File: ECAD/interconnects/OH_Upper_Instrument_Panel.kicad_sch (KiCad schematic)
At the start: 194 parts

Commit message: Closed issue #987, #988, & #992
Updated interconnect and PL.
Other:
- note added: "3.0 IN PIGTAILS ON 1A7A1J1/J2"

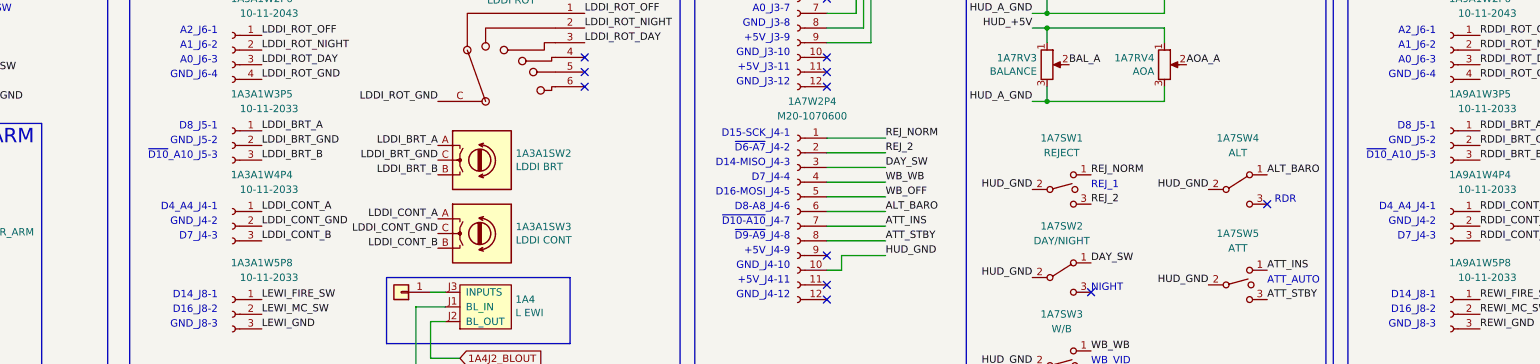
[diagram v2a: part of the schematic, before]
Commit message: Updated interconnect.
Made FCS_+5V NC
Reversed DDI BRT/CONT connections so they align properly with the PCB.
Closes #990 & #993
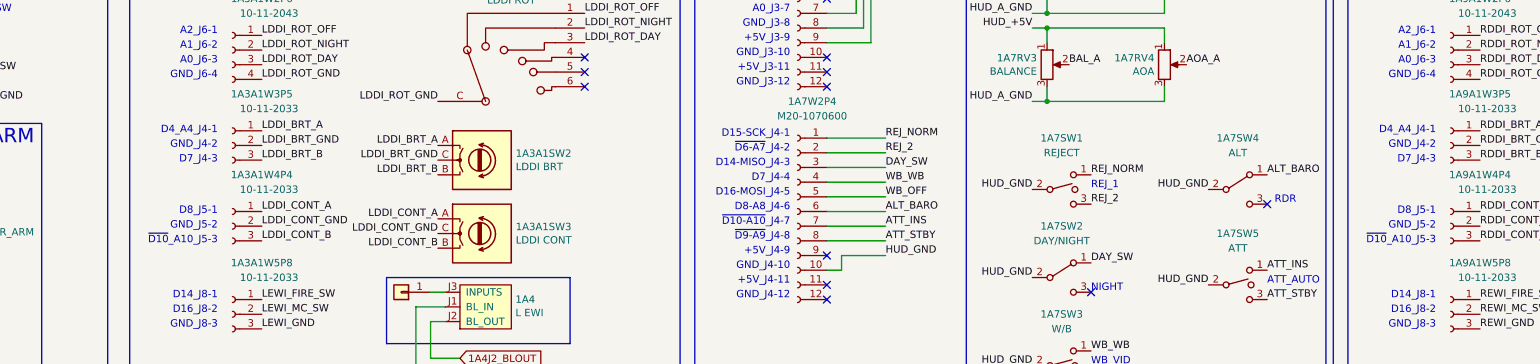
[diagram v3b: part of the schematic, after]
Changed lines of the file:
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@@
     (effects (font (size 1.27 1.27)) (justify right bottom))
   )
-  (text "~{D10}_A10_J5-3" (at 308.61 288.29 0)
+  (text "~{D10}_A10_J5-3" (at 308.61 302.895 0)
     (effects (font (size 1.27 1.27)) (justify right bottom))
   )
@@
     (effects (font (size 1.27 1.27)) (justify left bottom))
   )
-  (text "D8_J5-1" (at 519.43 283.21 0)
+  (text "D8_J5-1" (at 519.43 297.815 0)
     (effects (font (size 1.27 1.27)) (justify right bottom))
   )
@@
     (effects (font (size 1.27 1.27)) (justify right bottom))
   )
-  (text "D8_J5-1" (at 308.61 283.21 0)
+  (text "D8_J5-1" (at 308.61 297.815 0)
     (effects (font (size 1.27 1.27)) (justify right bottom))
   )
@@
     (effects (font (size 1.27 1.27)) (justify left bottom))
   )
-  (text "GND_J4-2" (at 519.43 299.72 0)
+  (text "GND_J4-2" (at 519.43 286.385 0)
     (effects (font (size 1.27 1.27)) (justify right bottom))
   )
@@
     (effects (font (size 1.27 1.27)) (justify right bottom))
   )
-  (text "D4_A4_J4-1" (at 308.61 297.18 0)
+  (text "D4_A4_J4-1" (at 308.61 283.845 0)
     (effects (font (size 1.27 1.27)) (justify right bottom))
   )
@@
     (effects (font (size 1.27 1.27)) (justify right bottom))
   )
-  (text "GND_J4-2" (at 308.61 299.72 0)
-    (effects (font (size 1.27 1.27)) (justify right bottom))
-  )
-  (text "D4_A4_J4-1" (at 519.43 297.18 0)
+  (text "GND_J4-2" (at 308.61 286.385 0)
+    (effects (font (size 1.27 1.27)) (justify right bottom))
+  )
+  (text "D4_A4_J4-1" (at 519.43 283.845 0)
     (effects (font (size 1.27 1.27)) (justify right bottom))
   )
@@
     (effects (font (size 1.27 1.27)) (justify left bottom))
   )
-  (text "~{D10}_A10_J5-3" (at 519.43 288.29 0)
+  (text "~{D10}_A10_J5-3" (at 519.43 302.895 0)
     (effects (font (size 1.27 1.27)) (justify right bottom))
   )
@@
     (effects (font (size 2.4892 2.4892)) (justify left bottom))
   )
-  (text "GND_J5-2" (at 308.61 285.75 0)
+  (text "GND_J5-2" (at 308.61 300.355 0)
     (effects (font (size 1.27 1.27)) (justify right bottom))
   )
@@
     (effects (font (size 1.27 1.27)) (justify left bottom))
   )
-  (text "D7_J4-3" (at 308.61 302.26 0)
+  (text "D7_J4-3" (at 308.61 288.925 0)
     (effects (font (size 1.27 1.27)) (justify right bottom))
   )
@@
     (effects (font (size 1.27 1.27)) (justify right bottom))
   )
-  (text "D7_J4-3" (at 519.43 302.26 0)
+  (text "D7_J4-3" (at 519.43 288.925 0)
     (effects (font (size 1.27 1.27)) (justify right bottom))
   )
@@
     (effects (font (size 1.27 1.27)) (justify right bottom))
   )
-  (text "GND_J5-2" (at 519.43 285.75 0)
-    (effects (font (size 1.27 1.27)) (justify right bottom))
-  )
+  (text "GND_J5-2" (at 519.43 300.355 0)
+    (effects (font (size 1.27 1.27)) (justify right bottom))
+  )

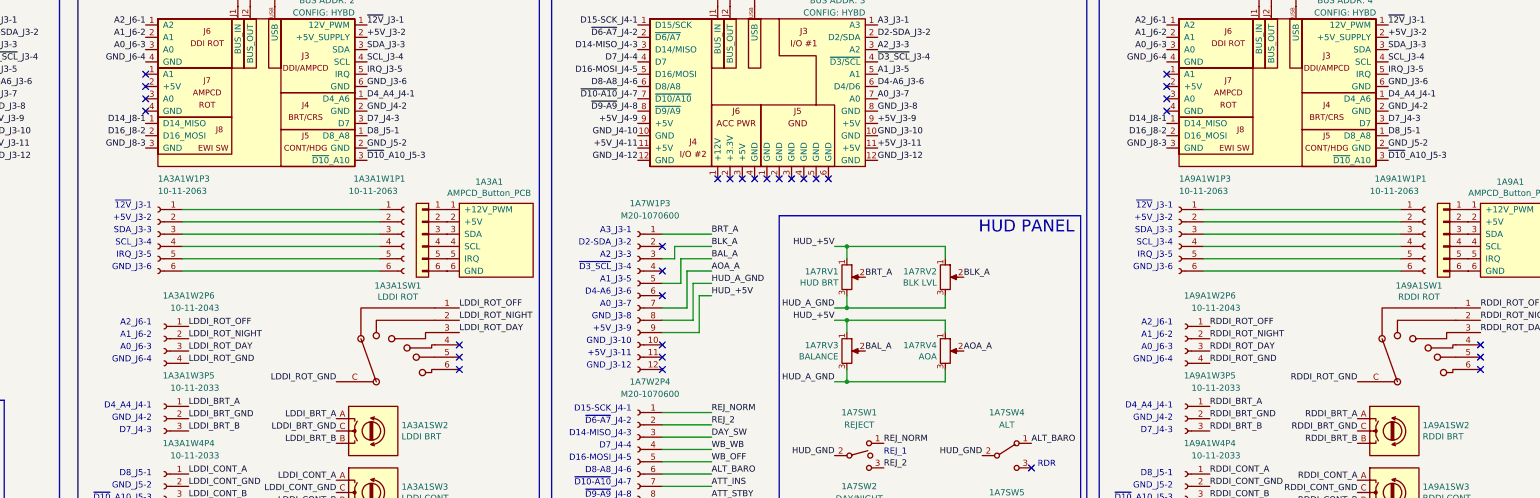
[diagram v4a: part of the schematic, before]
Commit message: Updated L/R-DDI and AMPCD controller net labels.
Revised interconnect to Rev A

1. SH 2:
    1. 1A3J4 Pin 1 WAS: D4_A4_J4-1 / IS: D4_A6_J4-1
    2. 1A3A1W3P5 Pin 1 WAS: D4_A4_J4-1 / IS: D4_A6_J4-1
    3. 1A9J4 Pin 1 WAS: D4_A4_J4-1 / IS: D4_A6_J4-1
    4. 1A9A1W3P5 Pin 1 WAS: D4_A4_J4-1 / IS: D4_A6_J4-1

2. SH 3:
    1. 2A3A1J4 Pin 1 WAS: D4_A4_J4-1 / IS: D4_A6_J4-1
    2. 2A3A1W4P1 Pin 1 WAS: D4_A4_J4-1 / IS: D4_A6_J4-1

Closes #1031
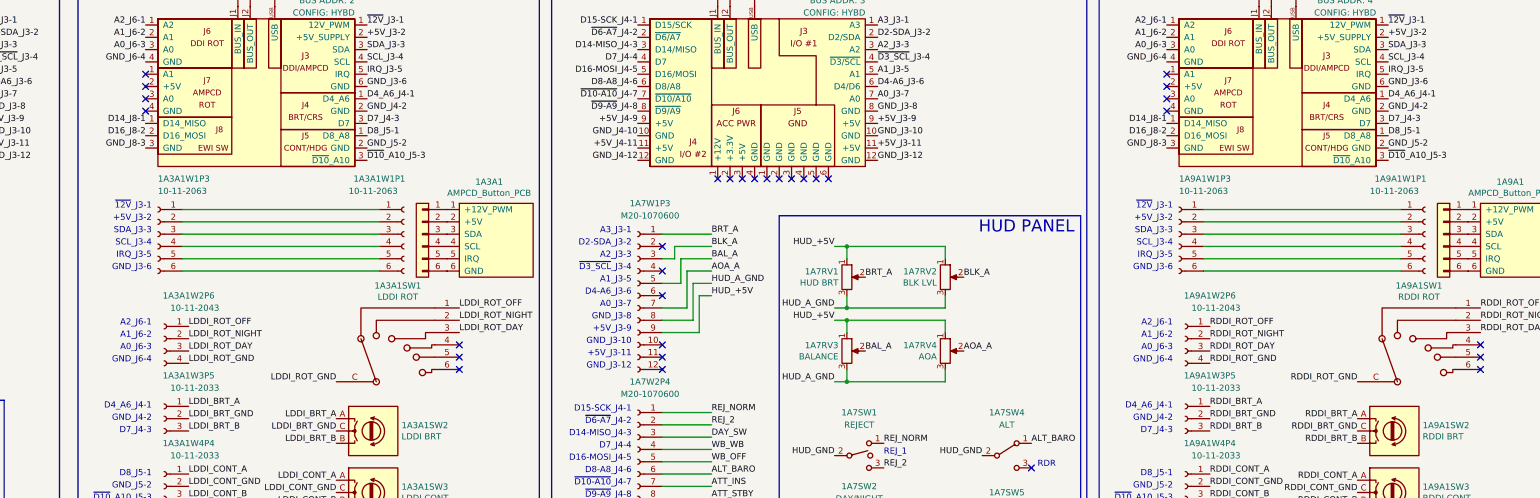
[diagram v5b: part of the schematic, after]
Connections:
- net D4_A4_J4-1 is gone; now on net ~{12V}_J3-1: 1A3.1 (D8_A8), 1A9.1 (D8_A8)
- new net D4_A6_J4-1: 1A3.1 (D8_A8), 1A9.1 (D8_A8)
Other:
- note added: "D4_A6_J4-1"
- note removed: "D4_A4_J4-1"
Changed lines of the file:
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@@
   (title_block
     (title "INTERCONNECT,")
-    (date "2023-06-10")
-    (rev "-")
+    (date "2024-02-29")
+    (rev "A")
     (company "OPENHORNET.COM")
     (comment 1 "OH-INTERCONNECT")
@@
     (effects (font (size 1.27 1.27)) (justify right bottom))
   )
-  (text "D4_A4_J4-1" (at 308.61 283.845 0)
+  (text "D4_A6_J4-1" (at 308.61 283.845 0)
     (effects (font (size 1.27 1.27)) (justify right bottom))
   )
@@
     (effects (font (size 1.27 1.27)) (justify right bottom))
   )
-  (text "D4_A4_J4-1" (at 519.43 283.845 0)
+  (text "D4_A6_J4-1" (at 519.43 283.845 0)
     (effects (font (size 1.27 1.27)) (justify right bottom))
   )
@@
     (effects (font (size 1.27 1.27)) (justify right bottom))
   )
-  (label "D4_A4_J4-1" (at 353.06 219.71 0) (fields_autoplaced)
+  (label "D4_A6_J4-1" (at 353.06 219.71 0) (fields_autoplaced)
     (effects (font (size 1.27 1.27)) (justify left bottom))
   )
@@
     (effects (font (size 1.27 1.27)) (justify left bottom))
   )
-  (label "D4_A4_J4-1" (at 563.88 219.71 0) (fields_autoplaced)
-    (effects (font (size 1.27 1.27)) (justify left bottom))
-  )
+  (label "D4_A6_J4-1" (at 563.88 219.71 0) (fields_autoplaced)
+    (effects (font (size 1.27 1.27)) (justify left bottom))
+  )
